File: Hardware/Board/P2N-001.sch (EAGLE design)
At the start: 34 parts, among them IC1 4053N, IC2 LTC485N, IC3 74LS07N, IC4 LTC485N, K1 G5V1, T1 2SC1815

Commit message: Added comment.
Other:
- note added: "1, 3: Vdd; 2, 4: GND 5: RST; 6: GND 7: LEDA; 8: LEDK"
- note added: "1: Sensor X; 2: Sensor Y 3: GPIO; 4: MISO 5: MOSI; 6: SCLCK"
- note added: "1: Vcc; 2: GND 3: Raw TX; 4: MIDI OUT Send; 5: MIDI OUT Return 6: Contact A; 7: GND; 8: Contact B 9: MIDI IN Anode; 10: MIDI IN Kathode"
- note removed: "1, 3: Vdd; 2, 4: GND 5: RST; 6: GND 7: LED; 7: R+GND"
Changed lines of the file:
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@@
 <text x="12.7" y="86.36" size="1.778" layer="91">1, 3: Vdd; 2, 4: GND
 5: RST; 6: GND
-7: LED; 7: R+GND</text>
+7: LEDA; 8: LEDK</text>
 <text x="10.16" y="152.4" size="1.778" layer="91" rot="R90">GeekPort II</text>
 <text x="132.08" y="167.64" size="1.778" layer="91">USB Bridge</text>
 <text x="48.26" y="88.9" size="1.778" layer="91">1: TXA; 2: TXK
 3: RXA; 4: RXK</text>
-<text x="314.96" y="88.9" size="1.778" layer="91">1: TX+; 2: TX-
+<text x="284.48" y="81.28" size="1.778" layer="91">1: TX+; 2: TX-
 3: RX+; 4: RX-</text>
+<text x="116.84" y="35.56" size="1.778" layer="91">1: Sensor X; 2: Sensor Y
+3: GPIO; 4: MISO
+5: MOSI; 6: SCLCK</text>
+<text x="284.48" y="134.62" size="1.778" layer="91">1: Vcc; 2: GND
+3: Raw TX; 4: MIDI OUT Send; 5: MIDI OUT Return
+6: Contact A; 7: GND; 8: Contact B
+9: MIDI IN Anode; 10: MIDI IN Kathode</text>
 </plain>
 <instances>

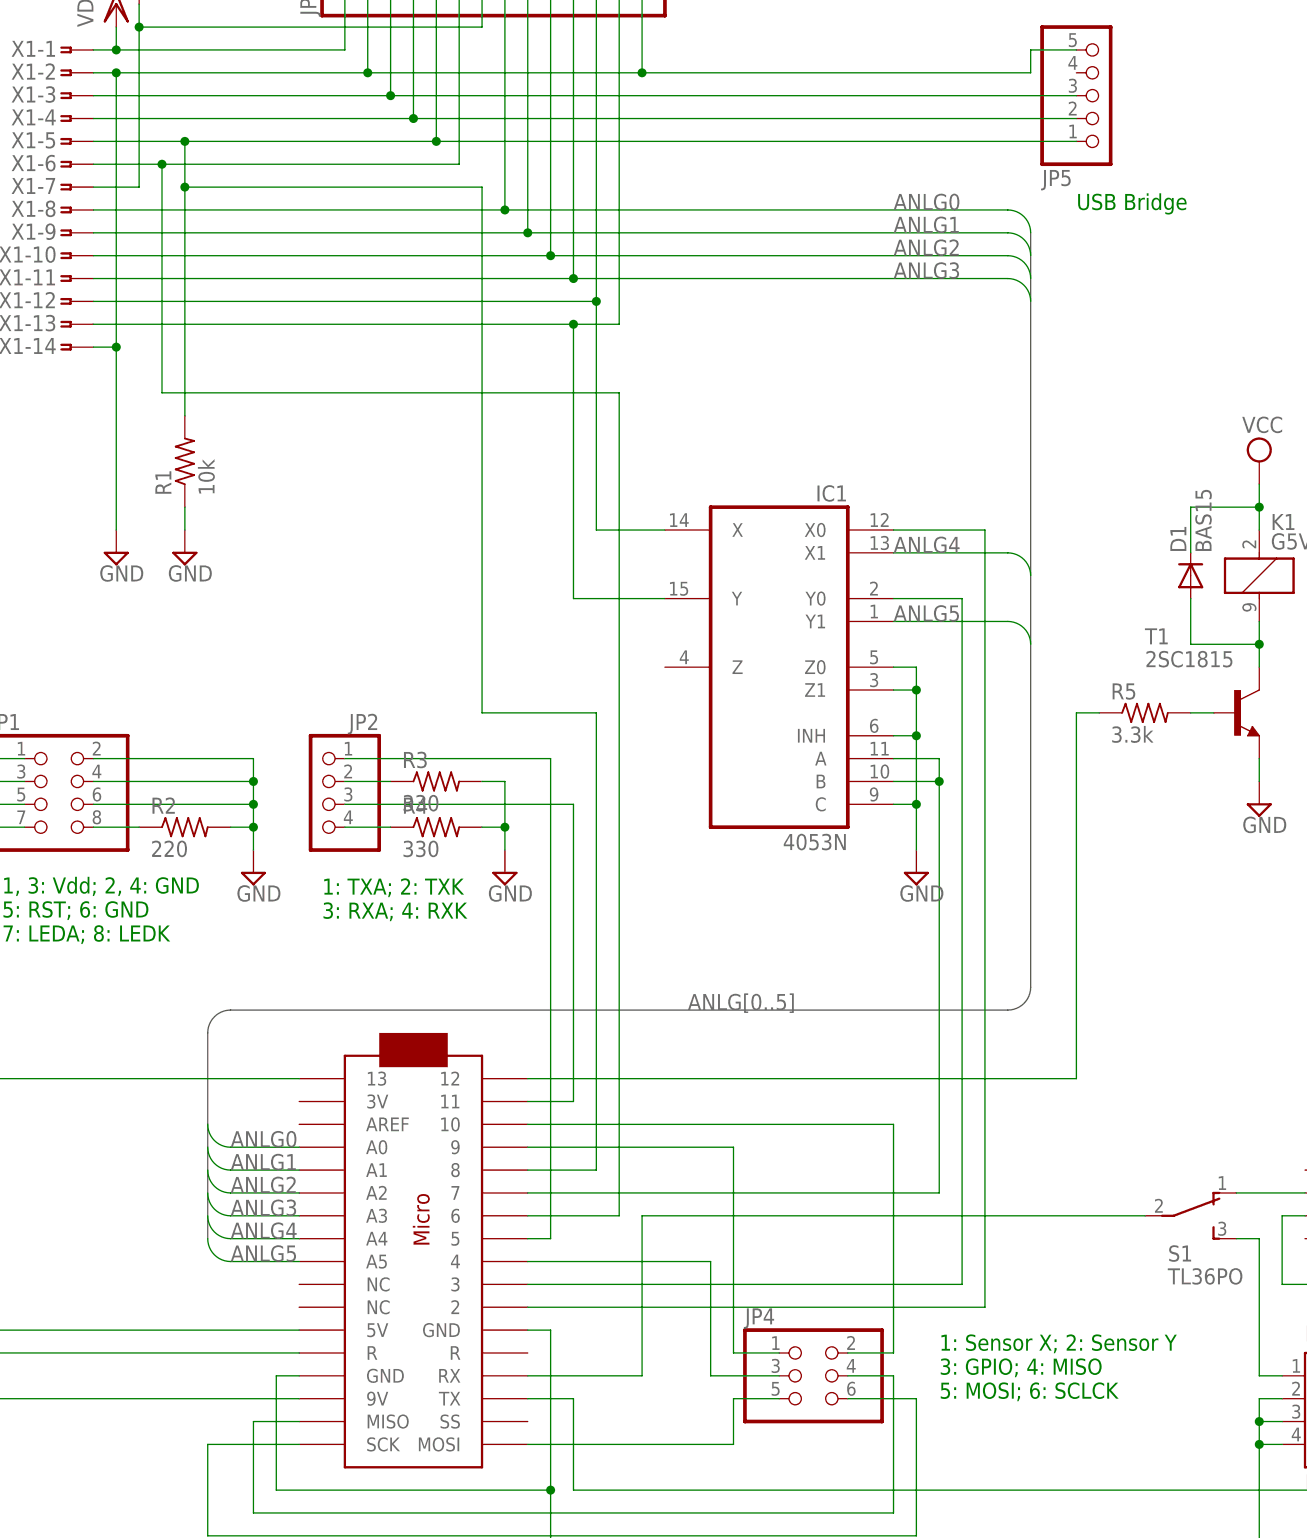
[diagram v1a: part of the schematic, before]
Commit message: Modified pinout.
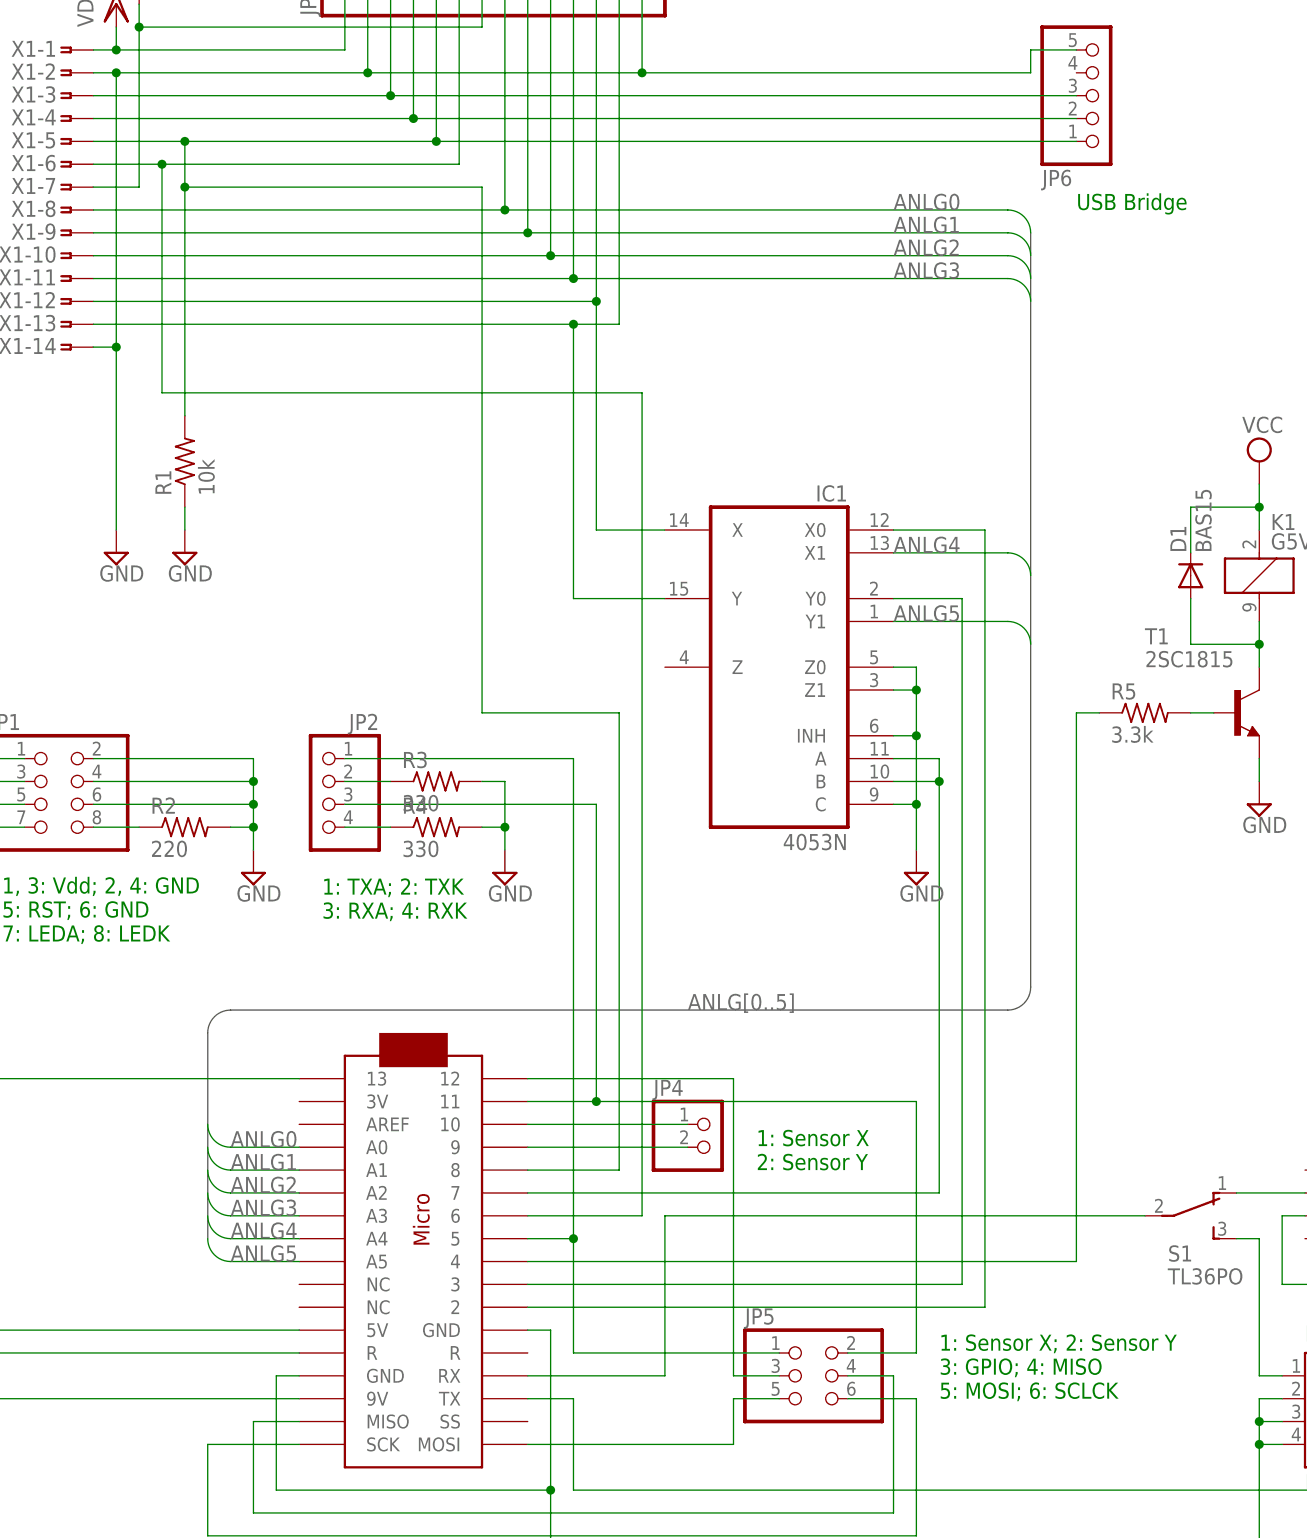
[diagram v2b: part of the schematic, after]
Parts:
- added JP6: (no value), pinhead:PINHD-1X5/90
- JP4: device pinhead:PINHD-2X3 -> pinhead:PINHD-1X2
- JP5: device pinhead:PINHD-1X5/90 -> pinhead:PINHD-2X3
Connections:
- removed net N$31: JP4.2, MC1.10
- new net N$34: MC1.4, R5.1
- net GND: now also JP6.5; no longer JP5.5
- net N$11: now also JP5.5; no longer JP4.5
- net N$13: now also JP5.6; no longer JP4.6
- net N$20: now also JP5.1
- net N$21: now also JP5.2
- net N$22: now also JP4.1, MC1.10; no longer MC1.12, R5.1
- net N$24: now also JP6.1; no longer JP5.1
- net N$25: now also JP6.2; no longer JP5.2
- net N$26: now also JP6.3; no longer JP5.3
- net N$30: now also JP4.2; no longer JP4.1
- net N$33: now also JP5.4; no longer JP4.4
- net N$9: now also JP5.3, MC1.12; no longer JP4.3, MC1.4
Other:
- note added: "1: Sensor X 2: Sensor Y"

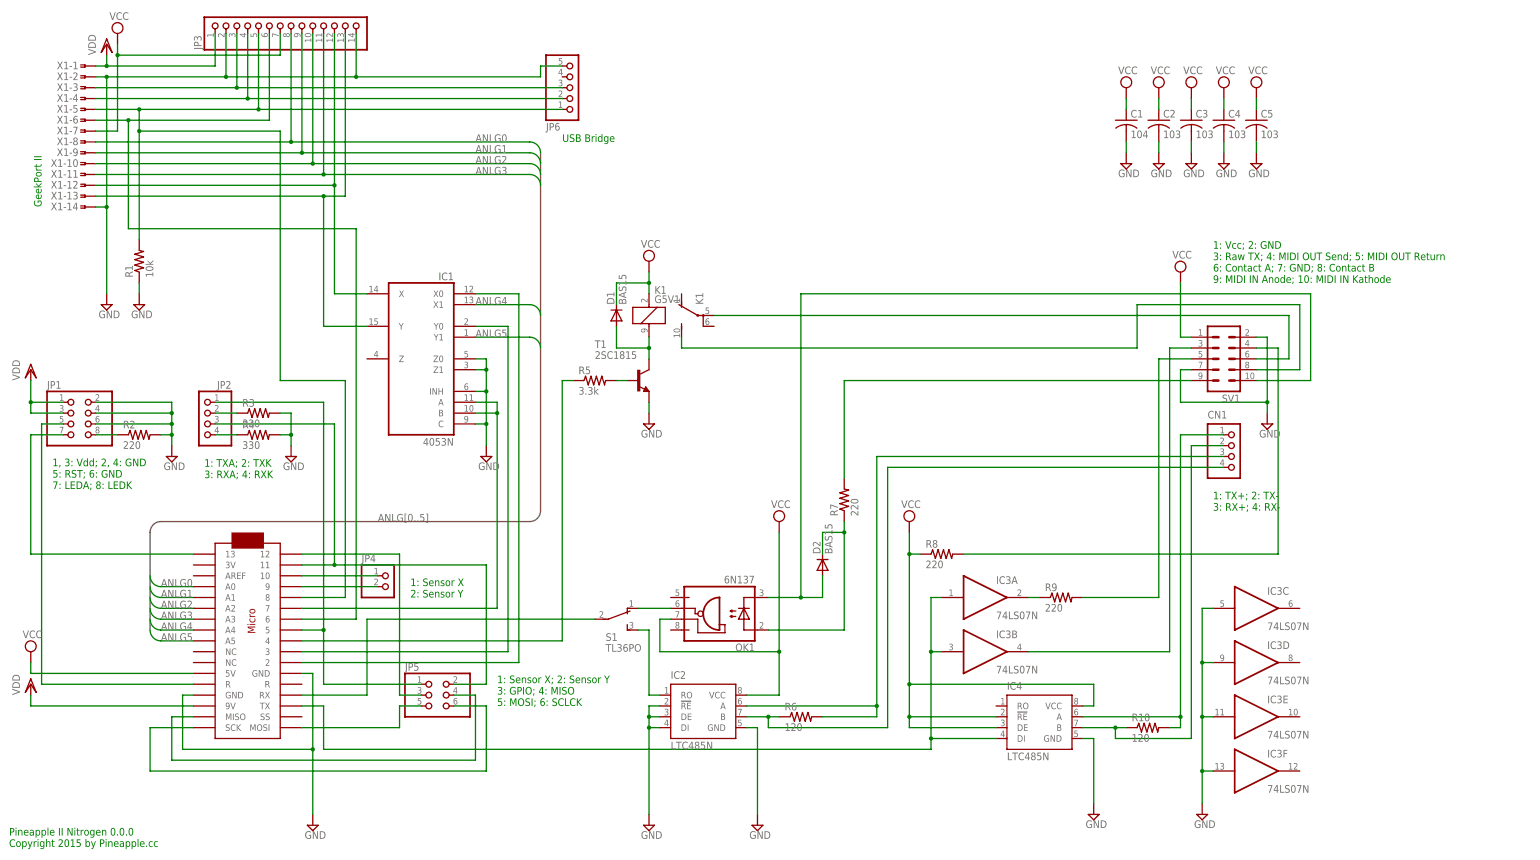
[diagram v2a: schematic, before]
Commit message: Labeled wires.
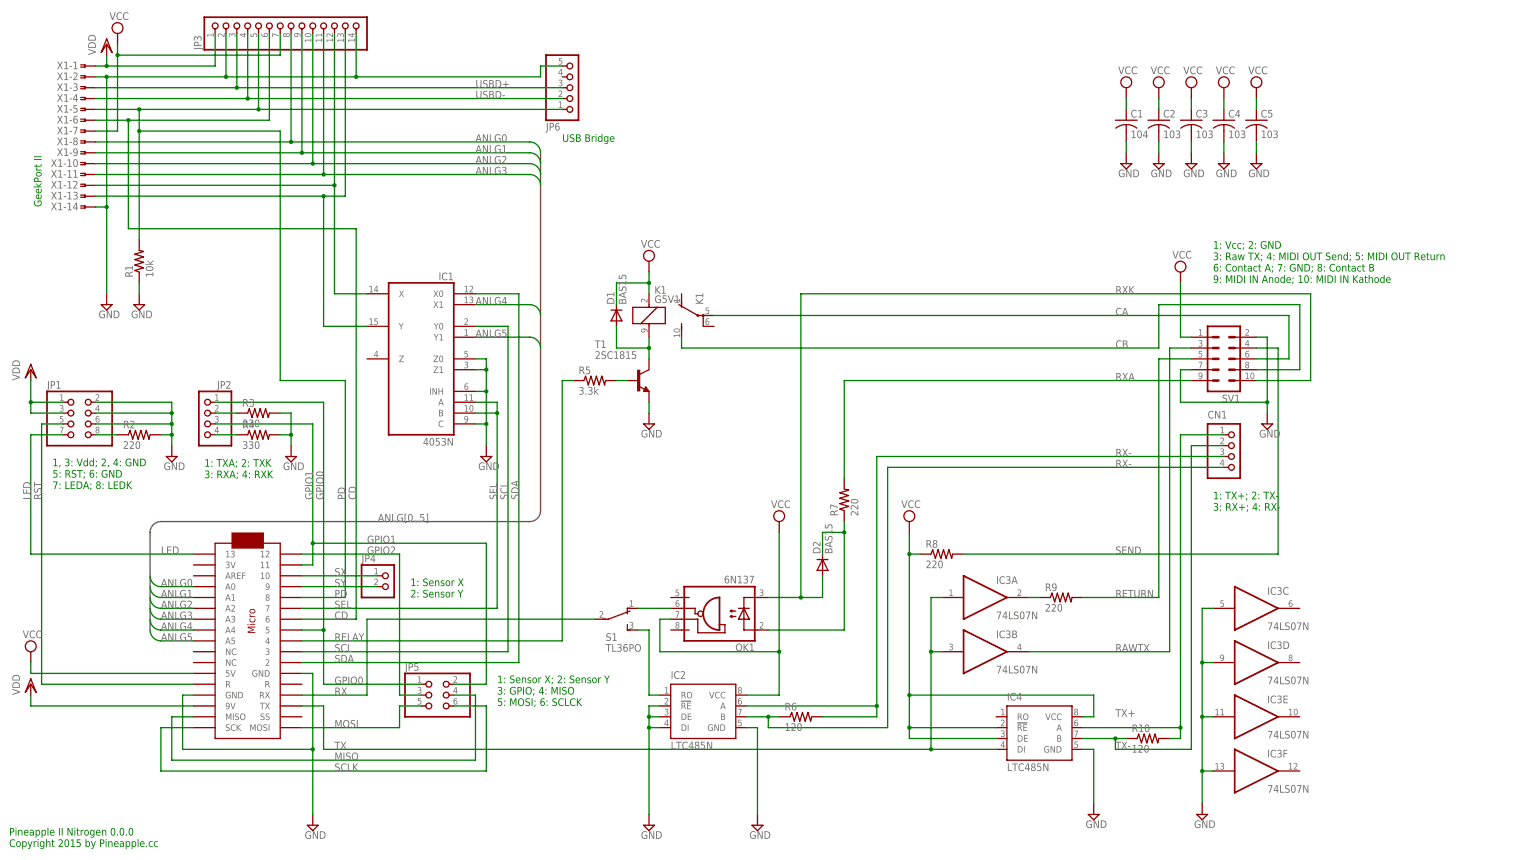
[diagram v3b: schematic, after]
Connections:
- net GEEK16 renamed SEL
- net MIDI1 renamed TX+
- net MIDI11 renamed RX+
- net MIDI13 renamed RX-
- net MIDI15 renamed RXK
- net MIDI3 renamed TX-
- net MIDI6 renamed TX
- net N$1 renamed RAWTX
- net N$10 renamed RETURN
- net N$11 renamed MOSI
- net N$12 renamed SEND
- net N$13 renamed SCLK
- net N$14 renamed CB
- net N$16 renamed CA
- net N$19 renamed SCL
- net N$20 renamed GPIO0
- net N$21 renamed GPIO1
- net N$22 renamed SX
- net N$23 renamed SDA
- net N$24 renamed PD
- net N$25 renamed USBD-
- net N$26 renamed USBD+
- net N$27 renamed CD
- net N$3 renamed RST
- net N$30 renamed SY
- net N$33 renamed MISO
- net N$34 renamed RELAY
- net N$4 renamed LED
- net N$5 renamed RXA
- net N$7 renamed RX
- net N$9 renamed GPIO2
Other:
- moved on the sheet: IC4, R10
